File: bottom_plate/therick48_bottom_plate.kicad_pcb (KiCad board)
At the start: 2 copper layers, 228 x 76 mm, 55 parts, among them U1 HOLE, U10 HOLE, U11 HOLE, U12 HOLE, U13 HOLE, U14 HOLE, U15 HOLE, U16 HOLE, U17 HOLE, U18 HOLE, U19 HOLE, U2 HOLE, U20 HOLE, U21 HOLE, U22 HOLE, U23 HOLE, U24 HOLE, U25 HOLE, U26 HOLE, U27 HOLE, U28 HOLE, U29 HOLE, U3 HOLE, U30 HOLE, U31 HOLE, U32 HOLE, U33 HOLE, U34 HOLE, U35 HOLE, U36 HOLE, U37 HOLE, U38 HOLE, U39 HOLE, U4 HOLE, U40 HOLE, U41 HOLE, U42 HOLE, U43 HOLE, U44 HOLE, U45 HOLE, U46 HOLE, U47 HOLE, U48 HOLE, U5 HOLE, U6 HOLE, U65 HOLE, U7 HOLE, U8 HOLE, U9 HOLE

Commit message: Add Gerbers
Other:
- outline, holes or cut-outs redrawn
- board text added: "therick48 Rev 1.0"
- board text removed: "therick"
- board text removed: "therick_19mm"
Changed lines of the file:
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@@
   (general
     (thickness 1.6)
-    (drawings 21)
+    (drawings 20)
     (tracks 0)
     (zones 0)
@@
     (pad 1 thru_hole circle (at 0 0) (size 3.5 3.5) (drill 2.2) (layers *.Cu *.Mask))
   )
-  (gr_text therick_19mm (at 50.16 91.96) (layer F.SilkS)
-    (effects (font (size 1 1) (thickness 0.15)) (justify left))
+  (gr_text "therick48 Rev 1.0" (at 48.639872 72.959808 90) (layer F.SilkS)
+    (effects (font (size 1.5 1.5) (thickness 0.2)))
   )
   (gr_line (start 274.36 38.76) (end 274.36 107.16) (layer Edge.Cuts) (width 0.15))
-  (gr_line (start 89.3 40.28) (end 89.3 34.96) (layer Edge.Cuts) (width 0.15))
-  (gr_line (start 79.42 40.28) (end 89.3 40.28) (layer Edge.Cuts) (width 0.15))
-  (gr_line (start 79.42 34.96) (end 79.42 40.28) (layer Edge.Cuts) (width 0.15))
+  (gr_line (start 89.299765 41.419891) (end 89.3 34.96) (layer Edge.Cuts) (width 0.15))
+  (gr_line (start 79.419765 41.419891) (end 89.299765 41.419891) (layer Edge.Cuts) (width 0.15))
+  (gr_line (start 79.42 34.96) (end 79.419791 41.419891) (layer Edge.Cuts) (width 0.15))
   (gr_line (start 50.16 110.96) (end 270.56 110.96) (layer Edge.Cuts) (width 0.15))
   (gr_line (start 46.36 38.76) (end 46.36 107.16) (layer Edge.Cuts) (width 0.15))
@@
   (gr_line (start 101.6 53.975) (end 104.775 53.975) (layer Dwgs.User) (width 0.15))
   (gr_line (start 103.1875 55.5625) (end 103.1875 51.59375) (layer Dwgs.User) (width 0.15))
-  (gr_text therick (at 218.12 109.474) (layer B.SilkS)
-    (effects (font (size 1.5 1.5) (thickness 0.2)) (justify left mirror))
-  )
 )

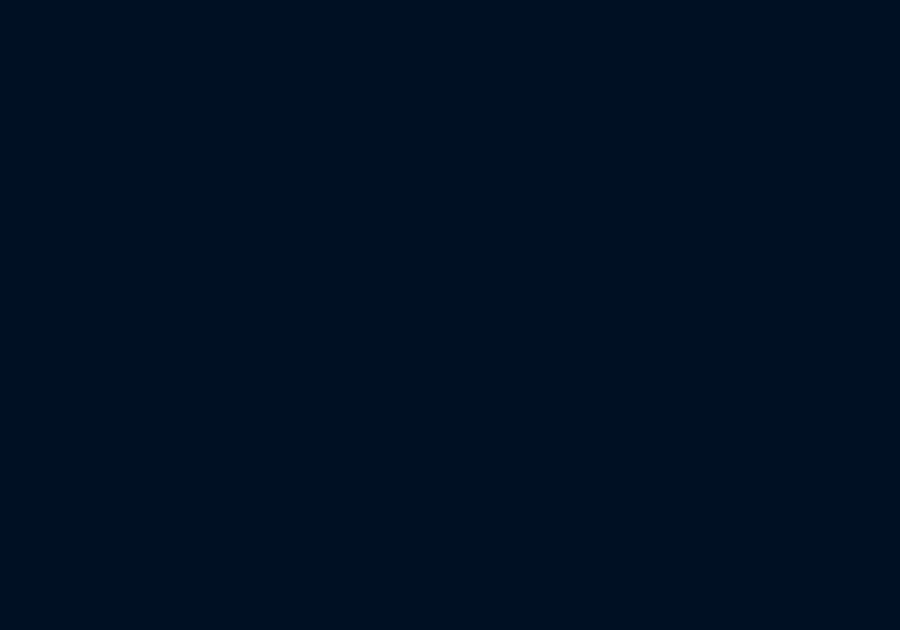
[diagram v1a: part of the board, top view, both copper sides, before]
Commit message: Add reset hole to bottom plate
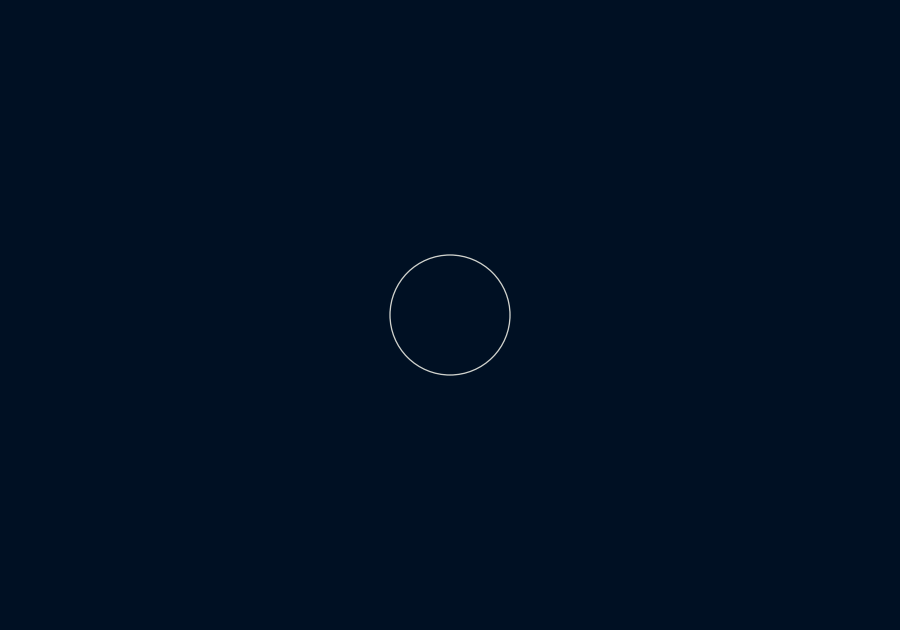
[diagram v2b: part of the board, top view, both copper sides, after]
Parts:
- added H7: MountingHole, random-keyboard-parts:Plate_hole_4mm, F.Cu at (122.4, 48.0)
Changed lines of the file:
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@@
     (tracks 0)
     (zones 0)
-    (modules 55)
+    (modules 56)
     (nets 1)
   )
@@
     (uvia_drill 0.2)
   )
+  (module random-keyboard-parts:Plate_hole_4mm (layer F.Cu)
+    (at 122.4153 47.9679)
+    (fp_text reference H7 (at -0.0127 1.2065) (layer Dwgs.User) hide
+      (effects (font (size 1 1) (thickness 0.15)))
+    )
+    (fp_text value MountingHole (at 0 -0.5) (layer F.Fab)
+      (effects (font (size 1 1) (thickness 0.15)))
+    )
+    (pad "" np_thru_hole circle (at 0.0127 -1.9939) (size 4 4) (drill 4) (layers *.Cu *.Mask))
+  )
   (module Keeb_footprints:MX100_outline (layer F.Cu)

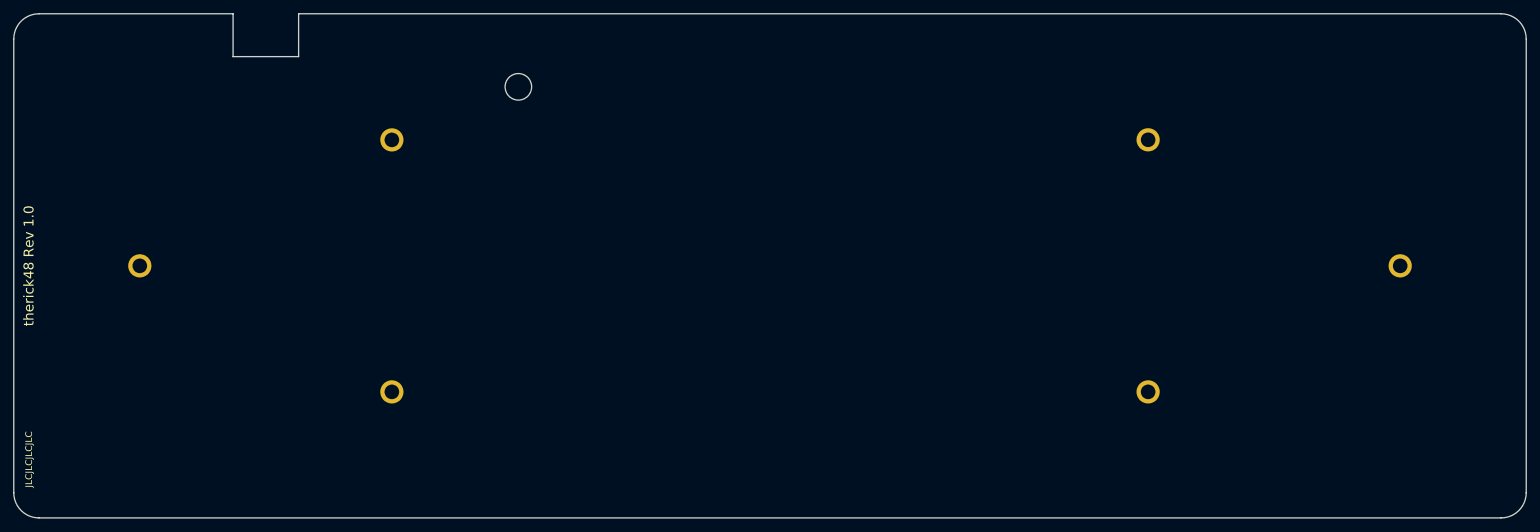
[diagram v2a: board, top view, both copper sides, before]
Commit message: Added more mounting holes
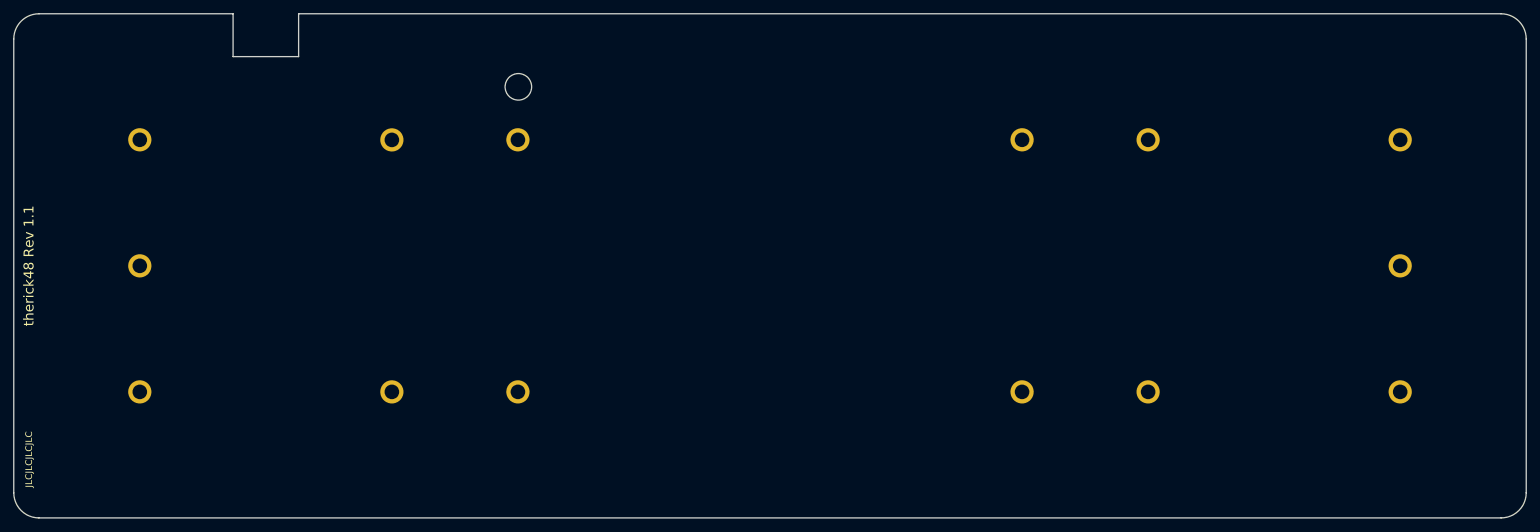
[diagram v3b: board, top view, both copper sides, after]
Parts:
- added H10: MountingHole, random-keyboard-parts:Generic-Mounthole, F.Cu at (122.4, 92.0)
- added H11: MountingHole, random-keyboard-parts:Generic-Mounthole, F.Cu at (122.4, 54.0)
- added H12: MountingHole, random-keyboard-parts:Generic-Mounthole, F.Cu at (198.4, 92.0)
- added H13: MountingHole, random-keyboard-parts:Generic-Mounthole, F.Cu at (198.4, 54.0)
- added H14: MountingHole, random-keyboard-parts:Generic-Mounthole, F.Cu at (255.4, 92.0)
- added H15: MountingHole, random-keyboard-parts:Generic-Mounthole, F.Cu at (255.4, 54.0)
- added H8: MountingHole, random-keyboard-parts:Generic-Mounthole, F.Cu at (65.4, 54.0)
- added H9: MountingHole, random-keyboard-parts:Generic-Mounthole, F.Cu at (65.4, 92.0)
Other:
- board text added: "therick48 Rev 1.1"
- board text removed: "therick48 Rev 1.0"
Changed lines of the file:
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@@
     (tracks 0)
     (zones 0)
-    (modules 56)
+    (modules 64)
     (nets 1)
   )
@@
     (uvia_drill 0.2)
   )
+  (module random-keyboard-parts:Generic-Mounthole (layer F.Cu)
+    (at 255.36 53.96)
+    (attr virtual)
+    (fp_text reference H15 (at 0 2) (layer Dwgs.User)
+      (effects (font (size 1 1) (thickness 0.15)))
+    )
+    (fp_text value MountingHole (at 0 -2) (layer Dwgs.User)
+      (effects (font (size 1 1) (thickness 0.15)))
+    )
+    (pad 1 thru_hole circle (at 0 0) (size 3.5 3.5) (drill 2.2) (layers *.Cu *.Mask))
+  )
+  (module random-keyboard-parts:Generic-Mounthole (layer F.Cu)
+    (at 255.36 91.96)
+    (attr virtual)
+    (fp_text reference H14 (at 0 2) (layer Dwgs.User)
+      (effects (font (size 1 1) (thickness 0.15)))
+    )
+    (fp_text value MountingHole (at 0 -2) (layer Dwgs.User)
+      (effects (font (size 1 1) (thickness 0.15)))
+    )
+    (pad 1 thru_hole circle (at 0 0) (size 3.5 3.5) (drill 2.2) (layers *.Cu *.Mask))
+  )
+  (module random-keyboard-parts:Generic-Mounthole (layer F.Cu)
+    (at 198.36 53.96)
+    (attr virtual)
+    (fp_text reference H13 (at 0 2) (layer Dwgs.User)
+      (effects (font (size 1 1) (thickness 0.15)))
+    )
+    (fp_text value MountingHole (at 0 -2) (layer Dwgs.User)
+      (effects (font (size 1 1) (thickness 0.15)))
+    )
+    (pad 1 thru_hole circle (at 0 0) (size 3.5 3.5) (drill 2.2) (layers *.Cu *.Mask))
+  )
+  (module random-keyboard-parts:Generic-Mounthole (layer F.Cu)
+    (at 198.36 91.96)
+    (attr virtual)
+    (fp_text reference H12 (at 0 2) (layer Dwgs.User)
+      (effects (font (size 1 1) (thickness 0.15)))
+    )
+    (fp_text value MountingHole (at 0 -2) (layer Dwgs.User)
+      (effects (font (size 1 1) (thickness 0.15)))
+    )
+    (pad 1 thru_hole circle (at 0 0) (size 3.5 3.5) (drill 2.2) (layers *.Cu *.Mask))
+  )
+  (module random-keyboard-parts:Generic-Mounthole (layer F.Cu)
+    (at 122.36 53.96)
+    (attr virtual)
+    (fp_text reference H11 (at 0 2) (layer Dwgs.User)
+      (effects (font (size 1 1) (thickness 0.15)))
+    )
+    (fp_text value MountingHole (at 0 -2) (layer Dwgs.User)
+      (effects (font (size 1 1) (thickness 0.15)))
+    )
+    (pad 1 thru_hole circle (at 0 0) (size 3.5 3.5) (drill 2.2) (layers *.Cu *.Mask))
+  )
+  (module random-keyboard-parts:Generic-Mounthole (layer F.Cu)
+    (at 122.36 91.96)
+    (attr virtual)
+    (fp_text reference H10 (at 0 2) (layer Dwgs.User)
+      (effects (font (size 1 1) (thickness 0.15)))
+    )
+    (fp_text value MountingHole (at 0 -2) (layer Dwgs.User)
+      (effects (font (size 1 1) (thickness 0.15)))
+    )
+    (pad 1 thru_hole circle (at 0 0) (size 3.5 3.5) (drill 2.2) (layers *.Cu *.Mask))
+  )
+  (module random-keyboard-parts:Generic-Mounthole (layer F.Cu)
+    (at 65.36 91.96)
+    (attr virtual)
+    (fp_text reference H9 (at 0 2) (layer Dwgs.User)
+      (effects (font (size 1 1) (thickness 0.15)))
+    )
+    (fp_text value MountingHole (at 0 -2) (layer Dwgs.User)
+      (effects (font (size 1 1) (thickness 0.15)))
+    )
+    (pad 1 thru_hole circle (at 0 0) (size 3.5 3.5) (drill 2.2) (layers *.Cu *.Mask))
+  )
+  (module random-keyboard-parts:Generic-Mounthole (layer F.Cu)
+    (at 65.36 53.96)
+    (attr virtual)
+    (fp_text reference H8 (at 0 2) (layer Dwgs.User)
+      (effects (font (size 1 1) (thickness 0.15)))
+    )
+    (fp_text value MountingHole (at 0 -2) (layer Dwgs.User)
+      (effects (font (size 1 1) (thickness 0.15)))
+    )
+    (pad 1 thru_hole circle (at 0 0) (size 3.5 3.5) (drill 2.2) (layers *.Cu *.Mask))
+  )
   (module random-keyboard-parts:Plate_hole_4mm (layer F.Cu)
     (at 122.4153 47.9679)
@@
     (pad 1 thru_hole circle (at 0 0) (size 3.5 3.5) (drill 2.2) (layers *.Cu *.Mask))
   )
-  (gr_text "therick48 Rev 1.0" (at 48.639872 72.959808 90) (layer F.SilkS)
+  (gr_text "therick48 Rev 1.1" (at 48.639872 72.959808 90) (layer F.SilkS)
     (effects (font (size 1.5 1.5) (thickness 0.2)))
   )

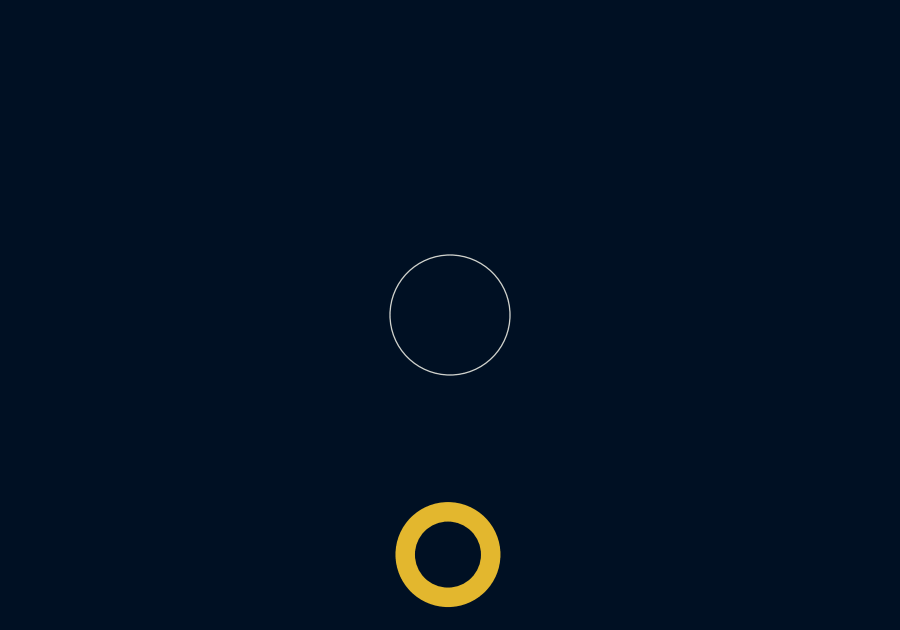
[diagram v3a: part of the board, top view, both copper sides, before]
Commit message: Add reset hole
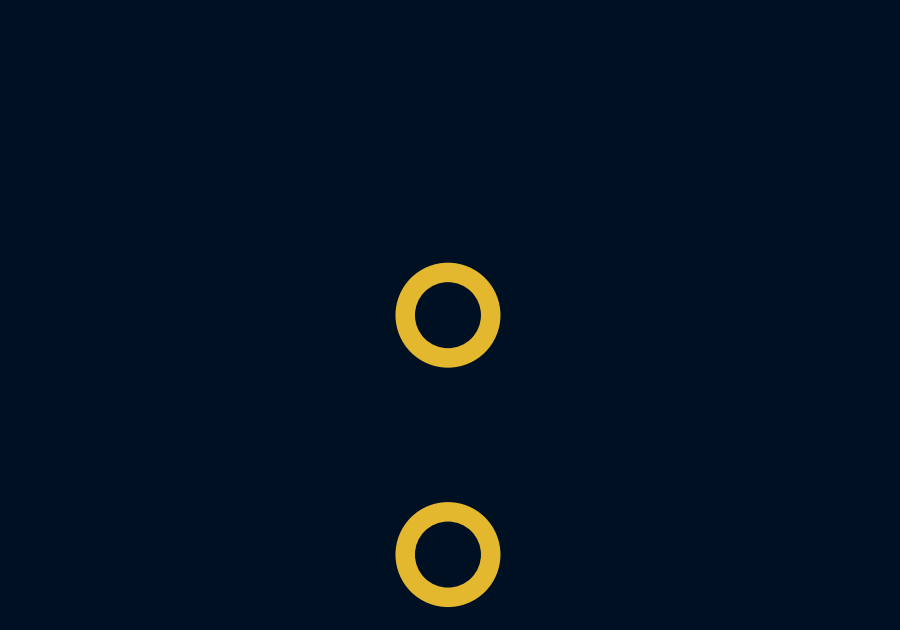
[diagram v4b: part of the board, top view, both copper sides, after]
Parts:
- H7: footprint random-keyboard-parts:Plate_hole_4mm -> random-keyboard-parts:Generic-Mounthole
- moved H7 1.99 mm to (122.4, 46.0)
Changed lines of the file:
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@@
+  )
+  (module random-keyboard-parts:Generic-Mounthole (layer F.Cu)
+    (at 122.36 45.98)
+    (attr virtual)
+    (fp_text reference H7 (at 0 2) (layer Dwgs.User)
+      (effects (font (size 1 1) (thickness 0.15)))
+    )
+    (fp_text value MountingHole (at 0 -2) (layer Dwgs.User)
+      (effects (font (size 1 1) (thickness 0.15)))
+    )
+    (pad 1 thru_hole circle (at 0 0) (size 3.5 3.5) (drill 2.2) (layers *.Cu *.Mask))
   )
   (module random-keyboard-parts:Generic-Mounthole (layer F.Cu)
@@
     (pad 1 thru_hole circle (at 0 0) (size 3.5 3.5) (drill 2.2) (layers *.Cu *.Mask))
   )
-  (module random-keyboard-parts:Plate_hole_4mm (layer F.Cu)
-    (at 122.4153 47.9679)
-    (fp_text reference H7 (at -0.0127 1.2065) (layer Dwgs.User) hide
-      (effects (font (size 1 1) (thickness 0.15)))
-    )
-    (fp_text value MountingHole (at 0 -0.5) (layer F.Fab)
-      (effects (font (size 1 1) (thickness 0.15)))
-    )
-    (pad "" np_thru_hole circle (at 0.0127 -1.9939) (size 4 4) (drill 4) (layers *.Cu *.Mask))
-  )
   (module Keeb_footprints:MX100_outline (layer F.Cu)

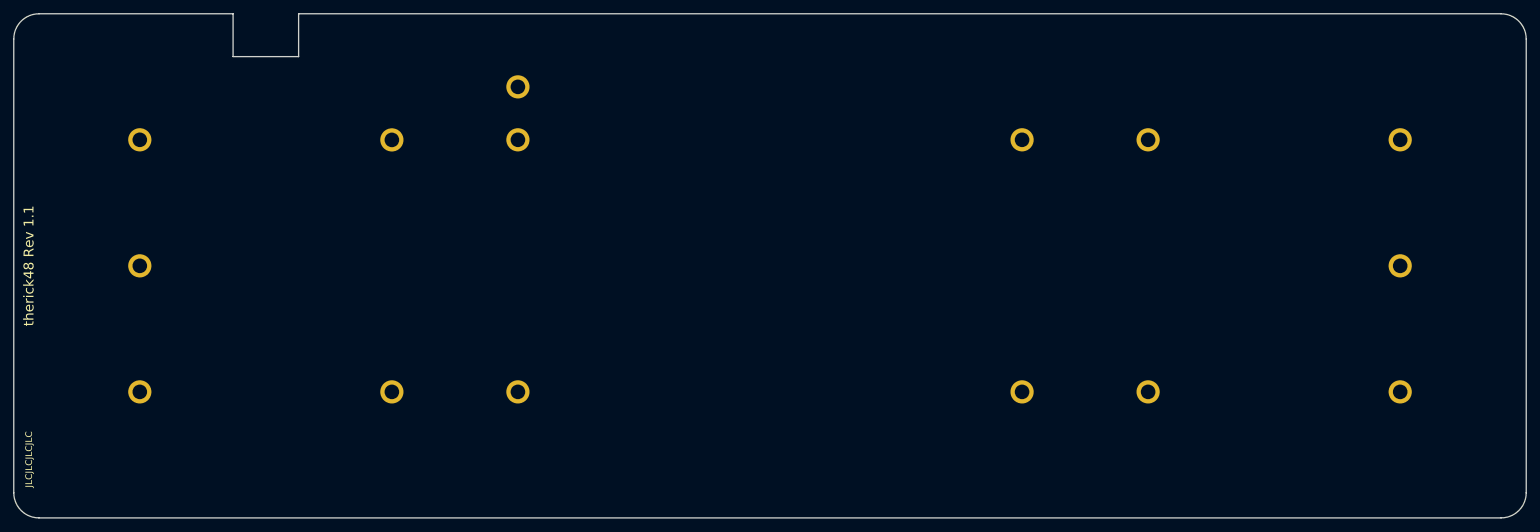
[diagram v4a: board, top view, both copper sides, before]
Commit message: Update bottom plate
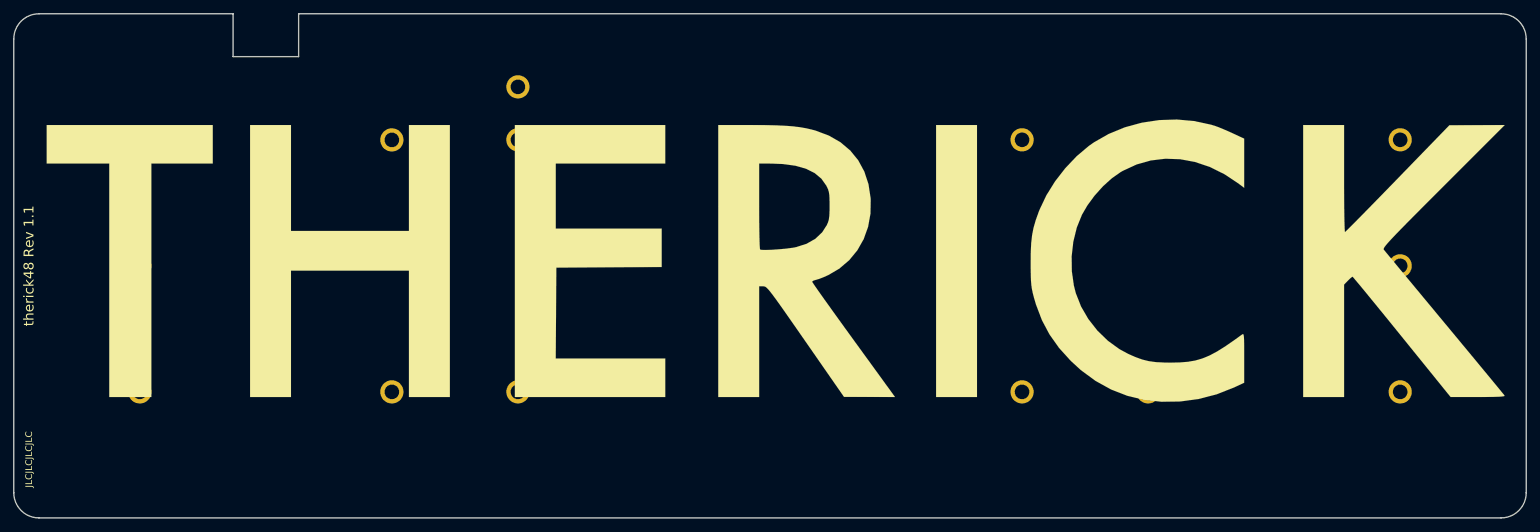
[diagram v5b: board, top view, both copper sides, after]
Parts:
- added U49: HOLE, Artwork:THERICK, F.Cu at (160.4, 73.0)
